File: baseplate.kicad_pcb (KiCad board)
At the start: 2 copper layers, 6 parts, among them U1 STM32L011F4Ux, U2 TLE5009E1000FUMA1, U3 DF52-4S-0.8H(21)

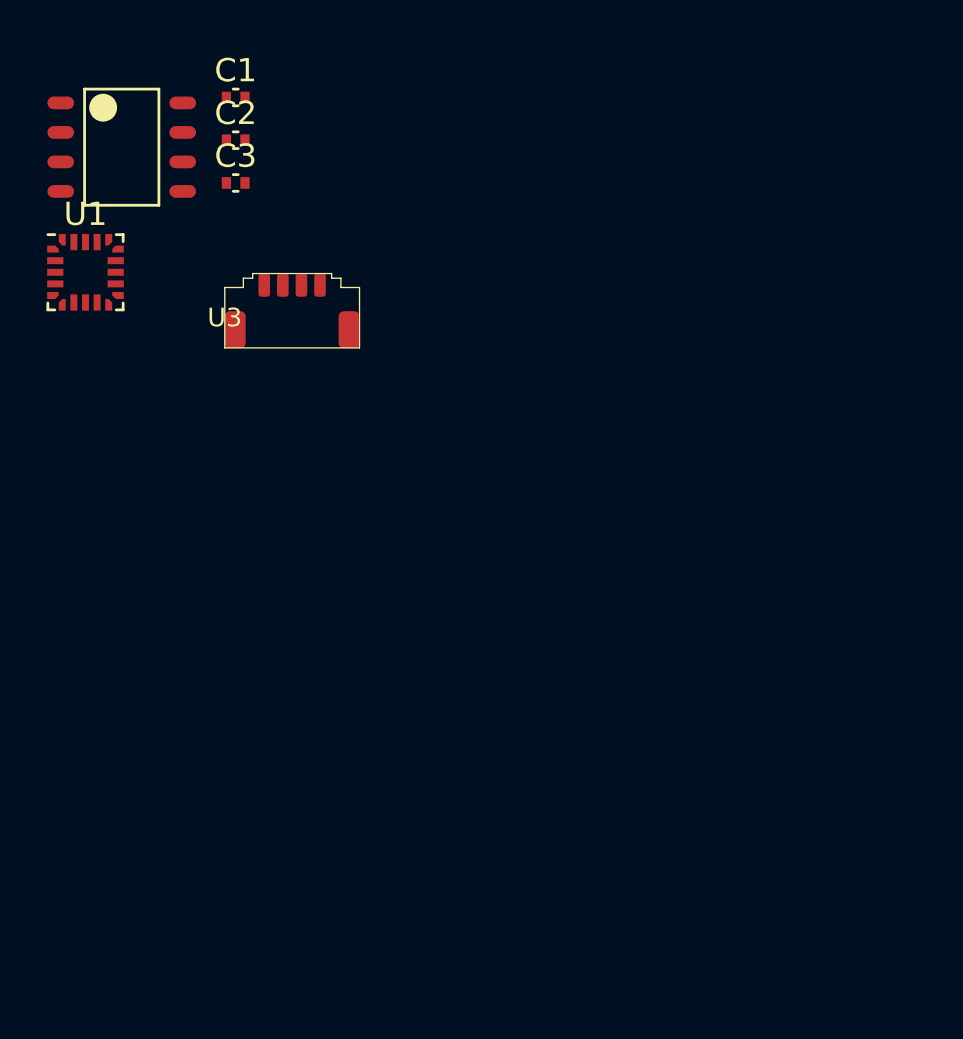
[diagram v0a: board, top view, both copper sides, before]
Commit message: dxfs copied over, baseplate pcb fully designed, more lib management
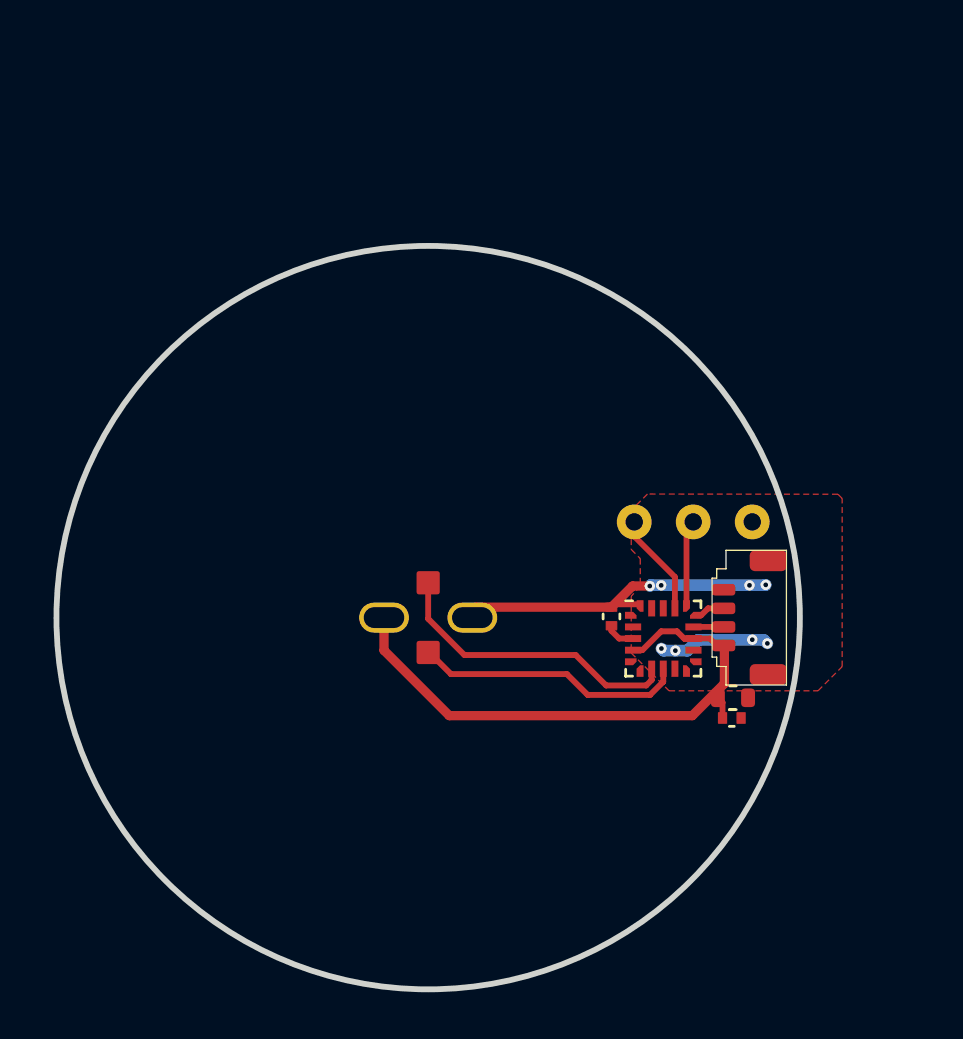
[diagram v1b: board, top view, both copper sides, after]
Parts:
- removed C3: 100nF, adapter-encoder:C_0402_1005Metric
- removed U2: TLE5009E1000FUMA1, adapter-encoder:SOIC8-TLE5009
- added C4: 4.7nF 0603, adapter-encoder:C_0603_1608Metric, F.Cu at (156.5, 105.5)
- added M1: THRU_HOLE_PAD, adapter-encoder:dogbone_slot, F.Cu at (141.5, 102.1)
- added M2: THRU_HOLE_PAD, adapter-encoder:dogbone_pad, F.Cu at (143.4, 100.6)
- added M3: THRU_HOLE_PAD, adapter-encoder:dogbone_pad, F.Cu at (143.4, 103.6)
- added M4: THRU_HOLE_PAD, adapter-encoder:dogbone_slot, F.Cu at (145.3, 102.1)
- added M5: THRU_HOLE_PAD, foc-pcb-library:PAD-BREADBOARD, F.Cu at (154.8, 98.0)
- added M6: THRU_HOLE_PAD, foc-pcb-library:PAD-BREADBOARD, F.Cu at (152.3, 98.0)
- added M7: THRU_HOLE_PAD, foc-pcb-library:PAD-BREADBOARD, F.Cu at (157.4, 98.0)
- C2: value 100nF -> 100nF 0402
- moved C2 32.8 mm to (156.5, 106.4)
- moved U1 29.4 mm to (153.5, 103.0)
- moved C1 27.6 mm to (151.3, 102.0), turned to 90 degrees
- moved U3 23.4 mm to (156.1, 102.1), turned to 90 degrees
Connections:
- C2 pad 1: /COS -> +3V3
- U1 pad 13: /3v3 -> +3V3
- U1 pad 4: /3v3 -> +3V3
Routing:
- net +3V3: track 0.00 -> 24.9 mm
- net GND: track 0.00 -> 19.5 mm, vias 0 -> 8
- net /SIN: track 0.00 -> 12.9 mm
- net /COS: track 0.00 -> 11.7 mm
- net /SWCLK: track 0.00 -> 4.44 mm
- net /SWDIO: track 0.00 -> 3.67 mm
- net /TX: track 0.00 -> 1.30 mm
- net Net-(U1-NRST): track 0.00 -> 1.29 mm
- net /RX: track 0.00 -> 1.25 mm
- added copper zone on F.Cu, net GND
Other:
- board outline added: 32 x 32 mm

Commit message: designed dogbone
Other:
- board text added: "+3V3"
- board text added: "COS"
- board text added: "GND"
- board text added: "SIN"
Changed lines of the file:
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@@
 (kicad_pcb (version 20221018) (generator pcbnew)
   (general
-    (thickness 1.6)
+    (thickness 1)
   )
   (paper "A4")
@@
   )
   (setup
+    (stackup
+      (layer "F.SilkS" (type "Top Silk Screen"))
+      (layer "F.Paste" (type "Top Solder Paste"))
+      (layer "F.Mask" (type "Top Solder Mask") (thickness 0.01))
+      (layer "F.Cu" (type "copper") (thickness 0.035))
+      (layer "dielectric 1" (type "core") (thickness 0.91) (material "FR4") (epsilon_r 4.5) (loss_tangent 0.02))
+      (layer "B.Cu" (type "copper") (thickness 0.035))
+      (layer "B.Mask" (type "Bottom Solder Mask") (thickness 0.01))
+      (layer "B.Paste" (type "Bottom Solder Paste"))
+      (layer "B.SilkS" (type "Bottom Silk Screen"))
+      (copper_finish "None")
+      (dielectric_constraints no)
+    )
     (pad_to_mask_clearance 0)
     (aux_axis_origin 143.415 102.1)
@@
   (gr_circle locked (center 143.415 102.1) (end 159.415 102.1)
     (stroke (width 0.25) (type solid)) (fill none) (layer "Edge.Cuts"))
+  (gr_text "COS" (at 142.525 105.17) (layer "F.SilkS")
+    (effects (font (size 0.5 0.5) (thickness 0.1) bold) (justify left bottom))
+  )
+  (gr_text "SIN" (at 142.715 99.79) (layer "F.SilkS")
+    (effects (font (size 0.5 0.5) (thickness 0.1) bold) (justify left bottom))
+  )
+  (gr_text "GND" (at 146.655 102.35) (layer "F.SilkS")
+    (effects (font (size 0.5 0.5) (thickness 0.1) bold) (justify left bottom))
+  )
+  (gr_text "+3V3" (at 138.065 102.39) (layer "F.SilkS")
+    (effects (font (size 0.5 0.5) (thickness 0.1) bold) (justify left bottom))
+  )
   (segment (start 151.305 102.45) (end 151.305 102.67) (width 0.254) (layer "F.Cu") (net 1))
   (segment (start 151.305 102.67) (end 151.635 103) (width 0.254) (layer "F.Cu") (net 1))

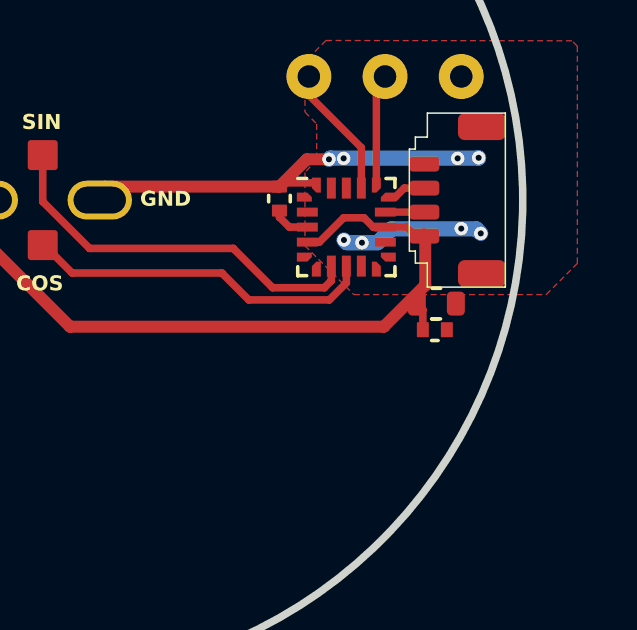
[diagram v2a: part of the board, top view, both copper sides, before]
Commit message: net labelling, silkscreen, boards finished
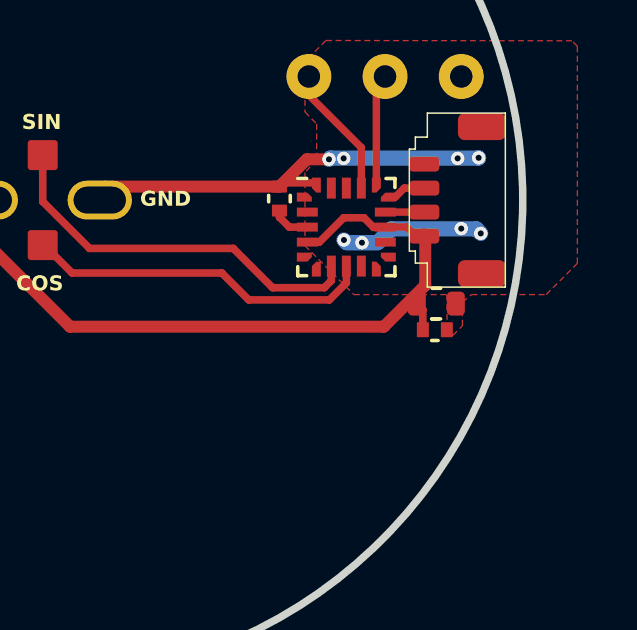
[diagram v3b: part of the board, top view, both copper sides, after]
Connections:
- M2 pad 1: /SIN -> /COS
- M3 pad 1: /COS -> /SIN
- U1 pad 7: /SIN -> /COS
- U1 pad 8: /COS -> /SIN
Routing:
- net /SIN: track 12.9 -> 11.7 mm
- net /COS: track 11.7 -> 12.9 mm
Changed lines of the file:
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@@
     )
     (pad "1" smd roundrect locked (at 0 0) (size 1 1) (layers "F.Cu" "F.Paste" "F.Mask") (roundrect_rratio 0.1)
-      (net 3 "/COS") (pinfunction "1") (pintype "passive") (thermal_bridge_angle 45))
+      (net 4 "/SIN") (pinfunction "1") (pintype "passive") (thermal_bridge_angle 45))
   )
   (footprint "adapter-encoder:C_0603_1608Metric" (layer "F.Cu")
@@
     )
     (pad "1" smd roundrect locked (at 0 0) (size 1 1) (layers "F.Cu" "F.Paste" "F.Mask") (roundrect_rratio 0.1)
-      (net 4 "/SIN") (pinfunction "1") (pintype "passive") (thermal_bridge_angle 45))
+      (net 3 "/COS") (pinfunction "1") (pintype "passive") (thermal_bridge_angle 45))
   )
   (footprint "adapter-encoder:ST_UFQFPN-20_3x3mm_P0.5mm" (layer "F.Cu")
@@
       ))
     (pad "7" smd rect (at -0.5 1.3) (size 0.3 0.7) (layers "F.Cu" "F.Paste" "F.Mask")
-      (net 4 "/SIN") (pinfunction "PA4") (pintype "bidirectional"))
+      (net 3 "/COS") (pinfunction "PA4") (pintype "bidirectional"))
     (pad "8" smd rect (at 0 1.3) (size 0.3 0.7) (layers "F.Cu" "F.Paste" "F.Mask")
-      (net 3 "/COS") (pinfunction "PA5") (pintype "bidirectional"))
+      (net 4 "/SIN") (pinfunction "PA5") (pintype "bidirectional"))
     (pad "9" smd rect (at 0.5 1.3) (size 0.3 0.7) (layers "F.Cu" "F.Paste" "F.Mask")
       (net 9 "unconnected-(U1-PA6-Pad9)") (pinfunction "PA6") (pintype "bidirectional+no_connect"))
@@
   (segment (start 153.545 103.52) (end 154.055 103.52) (width 0.508) (layer "B.Cu") (net 2))
   (segment (start 155.035 103.06) (end 157.865 103.06) (width 0.508) (layer "B.Cu") (net 2))
-  (segment (start 153.535 104.3) (end 153.535 104.86) (width 0.254) (layer "F.Cu") (net 3))
-  (segment (start 149.385 104.53) (end 144.395 104.53) (width 0.254) (layer "F.Cu") (net 3))
-  (segment (start 144.395 104.53) (end 143.465 103.6) (width 0.254) (layer "F.Cu") (net 3))
-  (segment (start 150.2814 105.4264) (end 149.385 104.53) (width 0.254) (layer "F.Cu") (net 3))
-  (segment (start 153.535 104.86) (end 152.9686 105.4264) (width 0.254) (layer "F.Cu") (net 3))
-  (segment (start 152.9686 105.4264) (end 150.2814 105.4264) (width 0.254) (layer "F.Cu") (net 3))
-  (segment (start 143.465 103.6) (end 143.415 103.6) (width 0.254) (layer "F.Cu") (net 3))
-  (segment (start 149.765 103.71) (end 144.975 103.71) (width 0.254) (layer "F.Cu") (net 4))
-  (segment (start 153.035 104.3) (end 153.035 104.785264) (width 0.254) (layer "F.Cu") (net 4))
-  (segment (start 151.075 105.02) (end 149.765 103.71) (width 0.254) (layer "F.Cu") (net 4))
-  (segment (start 143.415 102.15) (end 143.415 100.6) (width 0.254) (layer "F.Cu") (net 4))
-  (segment (start 152.800264 105.02) (end 151.075 105.02) (width 0.254) (layer "F.Cu") (net 4))
-  (segment (start 153.035 104.785264) (end 152.800264 105.02) (width 0.254) (layer "F.Cu") (net 4))
-  (segment (start 144.975 103.71) (end 143.415 102.15) (width 0.254) (layer "F.Cu") (net 4))
+  (segment (start 149.765 103.71) (end 144.975 103.71) (width 0.254) (layer "F.Cu") (net 3))
+  (segment (start 153.035 104.3) (end 153.035 104.785264) (width 0.254) (layer "F.Cu") (net 3))
+  (segment (start 151.075 105.02) (end 149.765 103.71) (width 0.254) (layer "F.Cu") (net 3))
+  (segment (start 143.415 102.15) (end 143.415 100.6) (width 0.254) (layer "F.Cu") (net 3))
+  (segment (start 152.800264 105.02) (end 151.075 105.02) (width 0.254) (layer "F.Cu") (net 3))
+  (segment (start 153.035 104.785264) (end 152.800264 105.02) (width 0.254) (layer "F.Cu") (net 3))
+  (segment (start 144.975 103.71) (end 143.415 102.15) (width 0.254) (layer "F.Cu") (net 3))
+  (segment (start 153.535 104.3) (end 153.535 104.86) (width 0.254) (layer "F.Cu") (net 4))
+  (segment (start 149.385 104.53) (end 144.395 104.53) (width 0.254) (layer "F.Cu") (net 4))
+  (segment (start 144.395 104.53) (end 143.465 103.6) (width 0.254) (layer "F.Cu") (net 4))
+  (segment (start 150.2814 105.4264) (end 149.385 104.53) (width 0.254) (layer "F.Cu") (net 4))
+  (segment (start 153.535 104.86) (end 152.9686 105.4264) (width 0.254) (layer "F.Cu") (net 4))
+  (segment (start 152.9686 105.4264) (end 150.2814 105.4264) (width 0.254) (layer "F.Cu") (net 4))
+  (segment (start 143.465 103.6) (end 143.415 103.6) (width 0.254) (layer "F.Cu") (net 4))
   (segment (start 154.835 102.5) (end 156.135 102.5) (width 0.25) (layer "F.Cu") (net 12))
   (segment (start 155.165 102) (end 155.465 101.7) (width 0.25) (layer "F.Cu") (net 13))
@@
         (xy 152.155 103.62)
         (xy 153.785 105.25)
+        (xy 156.885 105.25)
+        (xy 156.896725 106.61)
+        (xy 157.085 106.61)
+        (xy 157.405 106.29)
+        (xy 157.405 105.5)
+        (xy 157.705 105.25)
         (xy 160.195 105.25)
         (xy 161.235 104.21)

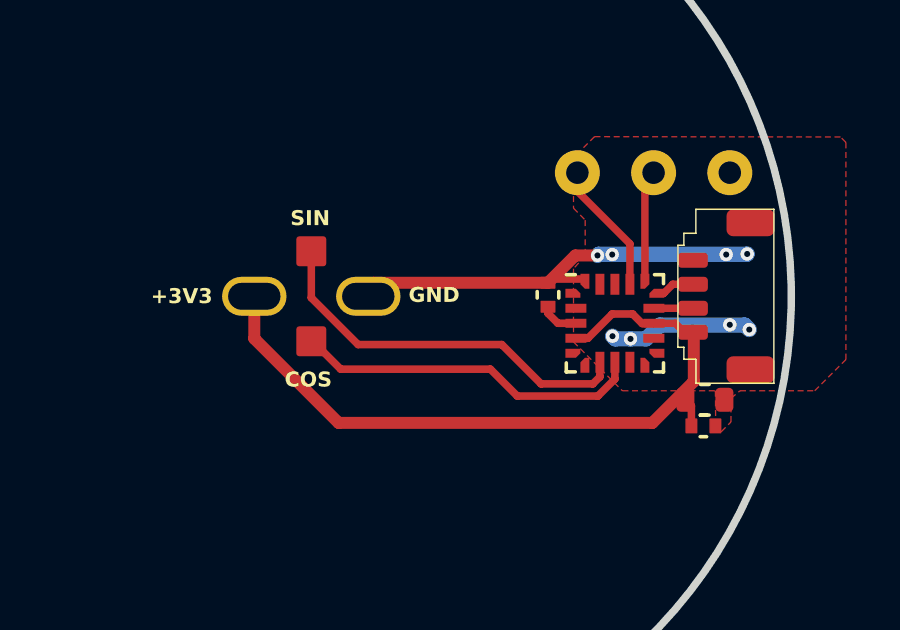
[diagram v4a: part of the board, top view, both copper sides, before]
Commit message: updated pad spacing for 1mm for dogbone and baseplate
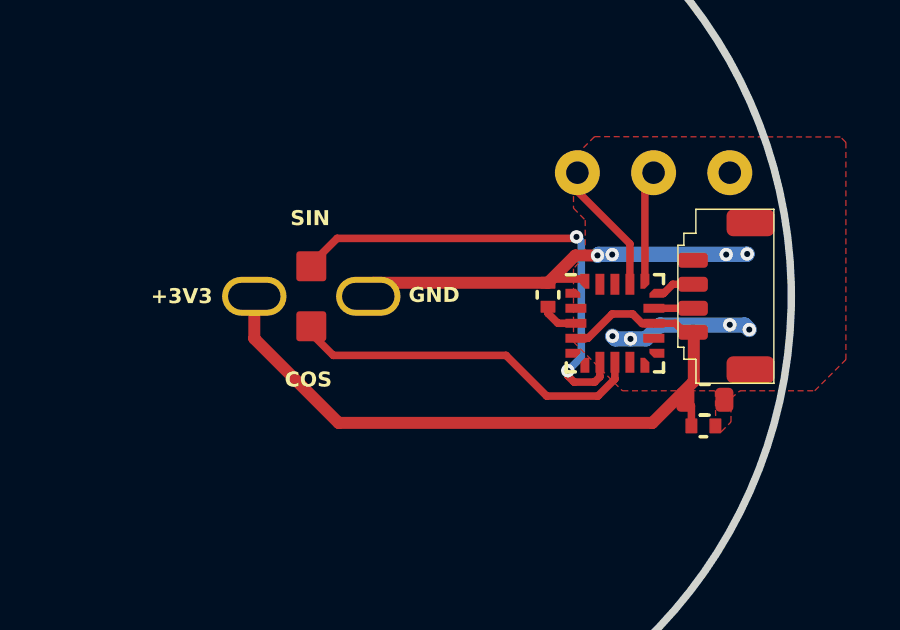
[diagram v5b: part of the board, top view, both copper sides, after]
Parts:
- moved M2 0.50 mm to (143.4, 101.1)
- moved M3 0.50 mm to (143.4, 103.1)
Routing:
- net /COS: track 12.9 -> 15.9 mm, vias 0 -> 2
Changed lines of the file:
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@@
   (net 18 "+3V3")
   (footprint "adapter-encoder:dogbone_pad" locked (layer "F.Cu")
-    (at 143.415 103.6)
+    (at 143.415 103.1)
     (property "Sheetfile" "baseplate.kicad_sch")
     (property "Sheetname" "")
@@
   )
   (footprint "adapter-encoder:dogbone_pad" locked (layer "F.Cu")
-    (at 143.415 100.6)
+    (at 143.415 101.1)
     (property "Sheetfile" "baseplate.kicad_sch")
     (property "Sheetname" "")
@@
   (segment (start 153.545 103.52) (end 154.055 103.52) (width 0.508) (layer "B.Cu") (net 2))
   (segment (start 155.035 103.06) (end 157.865 103.06) (width 0.508) (layer "B.Cu") (net 2))
-  (segment (start 149.765 103.71) (end 144.975 103.71) (width 0.254) (layer "F.Cu") (net 3))
-  (segment (start 153.035 104.3) (end 153.035 104.785264) (width 0.254) (layer "F.Cu") (net 3))
-  (segment (start 151.075 105.02) (end 149.765 103.71) (width 0.254) (layer "F.Cu") (net 3))
-  (segment (start 143.415 102.15) (end 143.415 100.6) (width 0.254) (layer "F.Cu") (net 3))
-  (segment (start 152.800264 105.02) (end 151.075 105.02) (width 0.254) (layer "F.Cu") (net 3))
-  (segment (start 153.035 104.785264) (end 152.800264 105.02) (width 0.254) (layer "F.Cu") (net 3))
-  (segment (start 144.975 103.71) (end 143.415 102.15) (width 0.254) (layer "F.Cu") (net 3))
+  (segment (start 152.205 100.17) (end 144.275 100.17) (width 0.254) (layer "F.Cu") (net 3))
+  (segment (start 152.175 104.96) (end 152.860264 104.96) (width 0.254) (layer "F.Cu") (net 3))
+  (segment (start 143.415 101.03) (end 143.415 101.1) (width 0.254) (layer "F.Cu") (net 3))
+  (segment (start 144.275 100.17) (end 143.415 101.03) (width 0.254) (layer "F.Cu") (net 3))
+  (segment (start 152.255 100.12) (end 152.205 100.17) (width 0.254) (layer "F.Cu") (net 3))
+  (segment (start 151.965 104.75) (end 152.175 104.96) (width 0.254) (layer "F.Cu") (net 3))
+  (segment (start 153.035 104.785264) (end 153.035 104.3) (width 0.254) (layer "F.Cu") (net 3))
+  (segment (start 152.860264 104.96) (end 153.035 104.785264) (width 0.254) (layer "F.Cu") (net 3))
+  (segment (start 151.965 104.58) (end 151.965 104.75) (width 0.254) (layer "F.Cu") (net 3))
+  (via (at 151.965 104.58) (size 0.45) (drill 0.2) (layers "F.Cu" "B.Cu") (net 3))
+  (via (at 152.255 100.12) (size 0.45) (drill 0.2) (layers "F.Cu" "B.Cu") (net 3))
+  (segment (start 152.255 100.12) (end 152.415 100.28) (width 0.254) (layer "B.Cu") (net 3))
+  (segment (start 152.415 104.13) (end 151.965 104.58) (width 0.254) (layer "B.Cu") (net 3))
+  (segment (start 152.415 100.28) (end 152.415 104.13) (width 0.254) (layer "B.Cu") (net 3))
+  (segment (start 153.535 104.86) (end 152.9686 105.4264) (width 0.254) (layer "F.Cu") (net 4))
+  (segment (start 149.905 104.07) (end 144.145 104.07) (width 0.254) (layer "F.Cu") (net 4))
+  (segment (start 151.2614 105.4264) (end 149.905 104.07) (width 0.254) (layer "F.Cu") (net 4))
+  (segment (start 144.145 104.07) (end 143.415 103.34) (width 0.254) (layer "F.Cu") (net 4))
+  (segment (start 143.415 103.34) (end 143.415 103.1) (width 0.254) (layer "F.Cu") (net 4))
+  (segment (start 152.9686 105.4264) (end 151.2614 105.4264) (width 0.254) (layer "F.Cu") (net 4))
   (segment (start 153.535 104.3) (end 153.535 104.86) (width 0.254) (layer "F.Cu") (net 4))
-  (segment (start 149.385 104.53) (end 144.395 104.53) (width 0.254) (layer "F.Cu") (net 4))
-  (segment (start 144.395 104.53) (end 143.465 103.6) (width 0.254) (layer "F.Cu") (net 4))
-  (segment (start 150.2814 105.4264) (end 149.385 104.53) (width 0.254) (layer "F.Cu") (net 4))
-  (segment (start 153.535 104.86) (end 152.9686 105.4264) (width 0.254) (layer "F.Cu") (net 4))
-  (segment (start 152.9686 105.4264) (end 150.2814 105.4264) (width 0.254) (layer "F.Cu") (net 4))
-  (segment (start 143.465 103.6) (end 143.415 103.6) (width 0.254) (layer "F.Cu") (net 4))
   (segment (start 154.835 102.5) (end 156.135 102.5) (width 0.25) (layer "F.Cu") (net 12))
   (segment (start 155.165 102) (end 155.465 101.7) (width 0.25) (layer "F.Cu") (net 13))
